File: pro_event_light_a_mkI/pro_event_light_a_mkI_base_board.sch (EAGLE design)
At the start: 29 parts, among them IC1 ILD4001, IC2 ILD4001, IC3 ILD4001, IC4 ILD4001

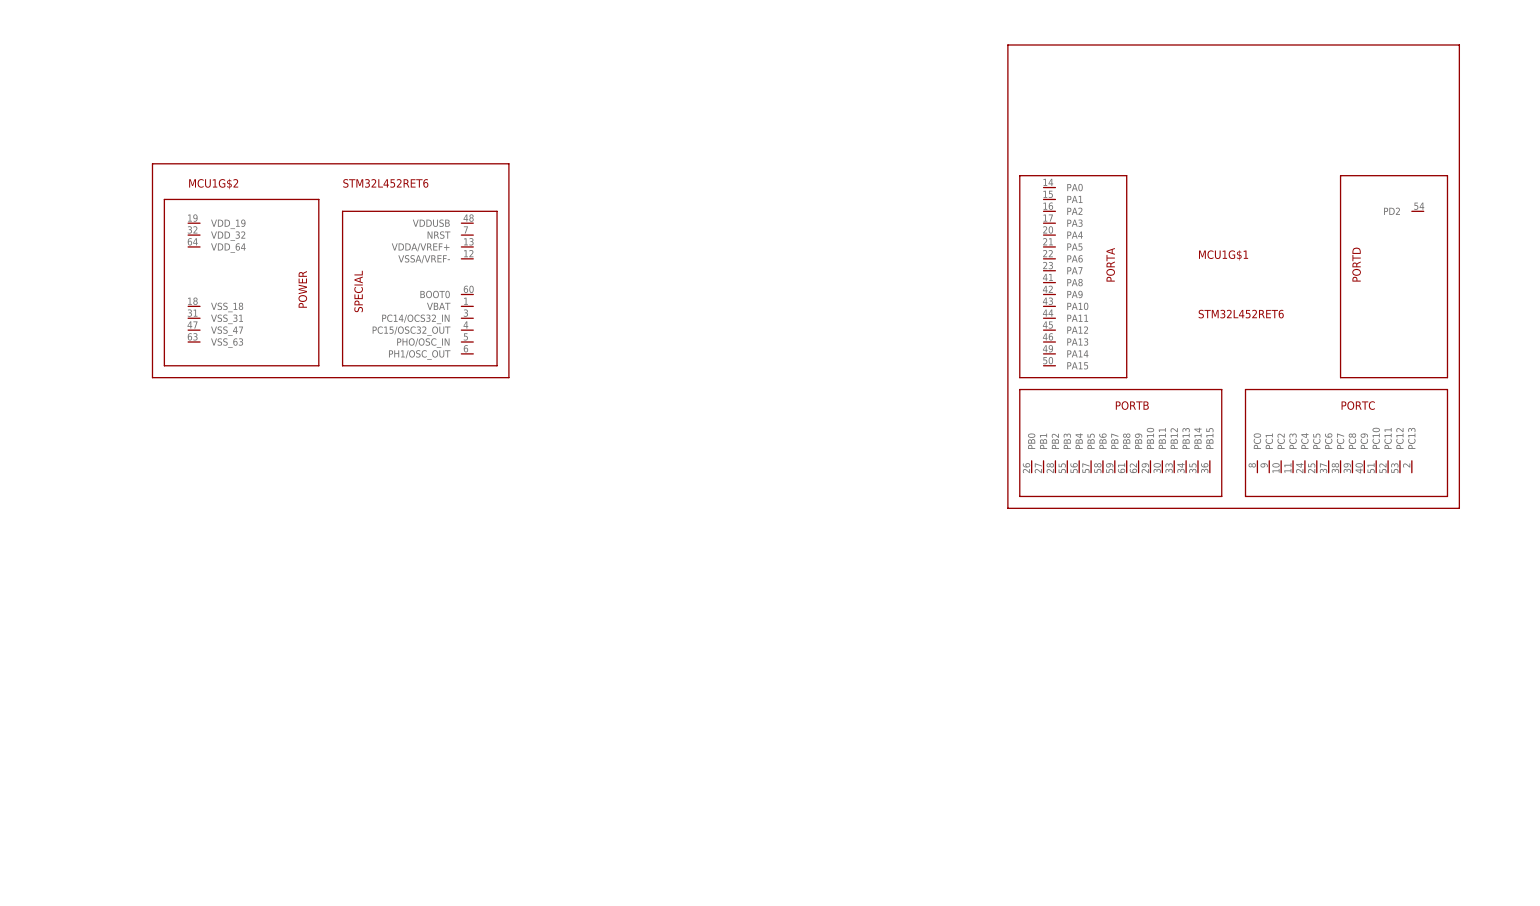
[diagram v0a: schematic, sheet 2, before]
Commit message: included rotary switch (also in separate library)
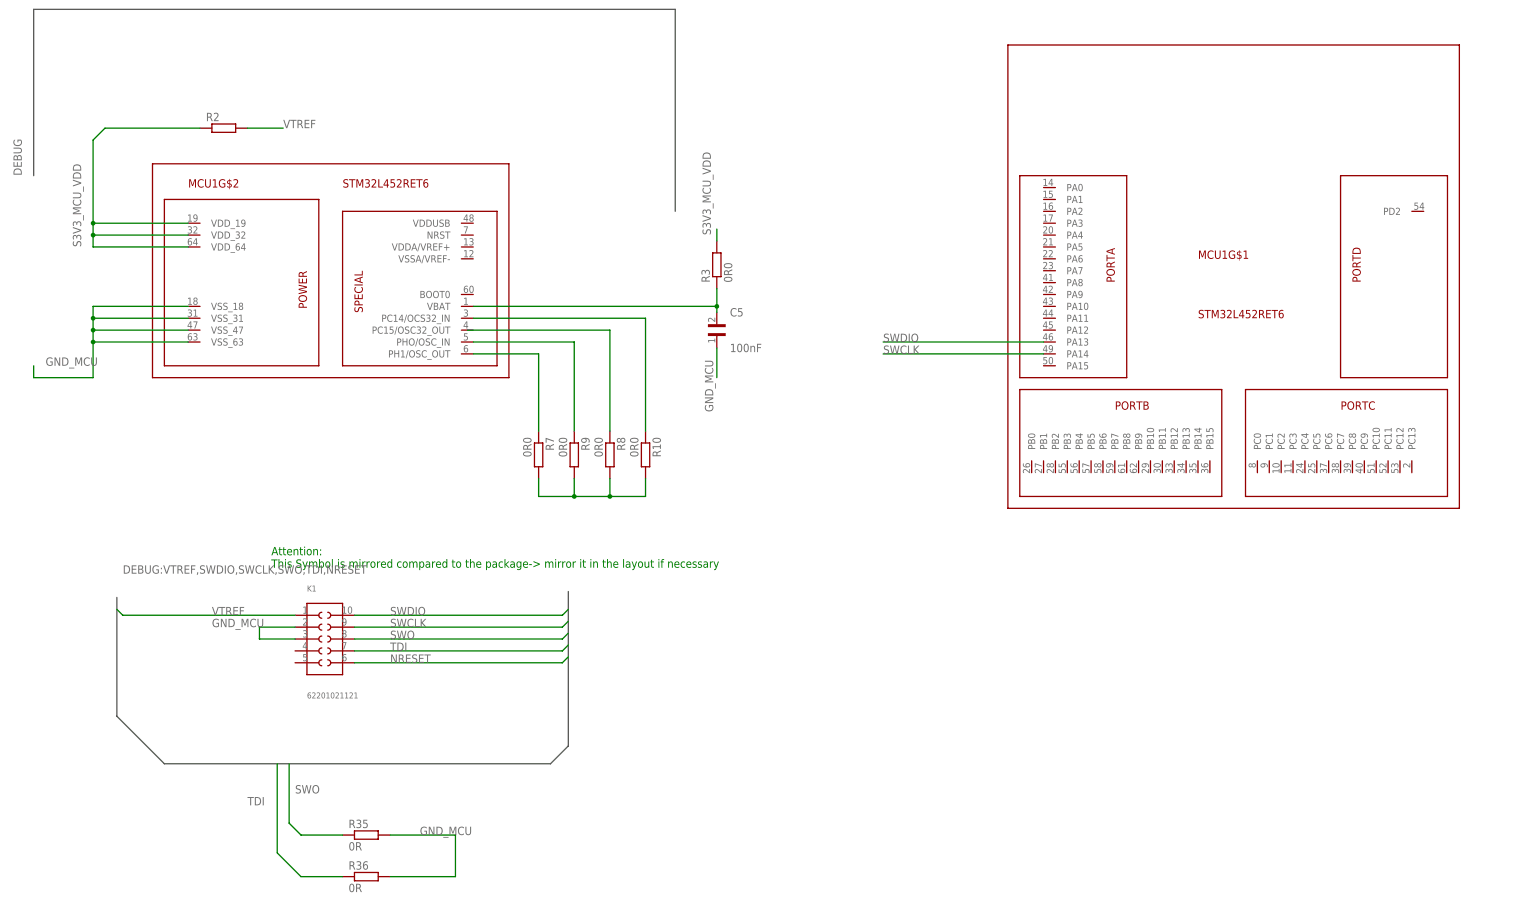
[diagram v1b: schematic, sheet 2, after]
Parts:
- added C1, C29, C34, C35: 1uF, Eagle_Wurth_Elektronik_Passive_Capacitors_rev15a:WCAP-CSGP_1206
- added C5: 100nF, Eagle_Wurth_Elektronik_Passive_Capacitors_rev15a:WCAP-CSGP_0603-REFLOW
- added K1: 62201021121, Board_to_Board_Connectors_rev15d:62201021121
- added R10, R3, R7, R8, R9: 0R0, rcl:R-EU_R0603
- added R2: (no value), rcl:R-EU_R0603
- added R35, R36: 0R, rcl:R-EU_R0603
- added U$10, U$11, U$15, U$8: (no value), mod-eagle_library_standard_passive_parts:PCB_MOUNTING_HOLES_M3
- added U$7: ALPS_EC11D, mod_eagle_library_switches:ALPS_EC11D
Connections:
- new net GND_MCU: C1.2, C29.2, C34.2, C35.2, C5.1, K1.2, K1.3, MCU1G$2.VSS_18, MCU1G$2.VSS_47, MCU1G$2.VSS_63, R10.2, R35.2, R36.2, R7.2, R8.2, R9.2
- new net N$15: C34.1, U$10.1
- new net N$17: C35.1, U$15.1
- new net N$18: C1.1, U$8.1
- new net N$19: C5.2, MCU1G$2.VBAT, R3.1
- new net N$20: MCU1G$2.PC14/OCS32_IN, R10.1
- new net N$21: R8.1
- new net N$26: MCU1G$2.PHO/OSC_IN, R9.1
- new net N$27: MCU1G$2.PH1/OSC_OUT, R7.1
- new net N$9: C29.1, U$11.1
- new net NRESET: K1.6
- new net S3V3_MCU_VDD: MCU1G$2.VDD_19, MCU1G$2.VDD_32, MCU1G$2.VDD_64, R2.1, R3.2
- new net SWCLK: K1.9, MCU1G$1.PA14
- new net SWDIO: K1.10, MCU1G$1.PA13
- new net SWO: K1.8, R35.1
- new net TDI: K1.7, R36.1
- new net VTREF: K1.1, R2.2
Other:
- note added: "Attention: This Symbol is mirrored compared to the package-> mirror it in the layout if necessary"

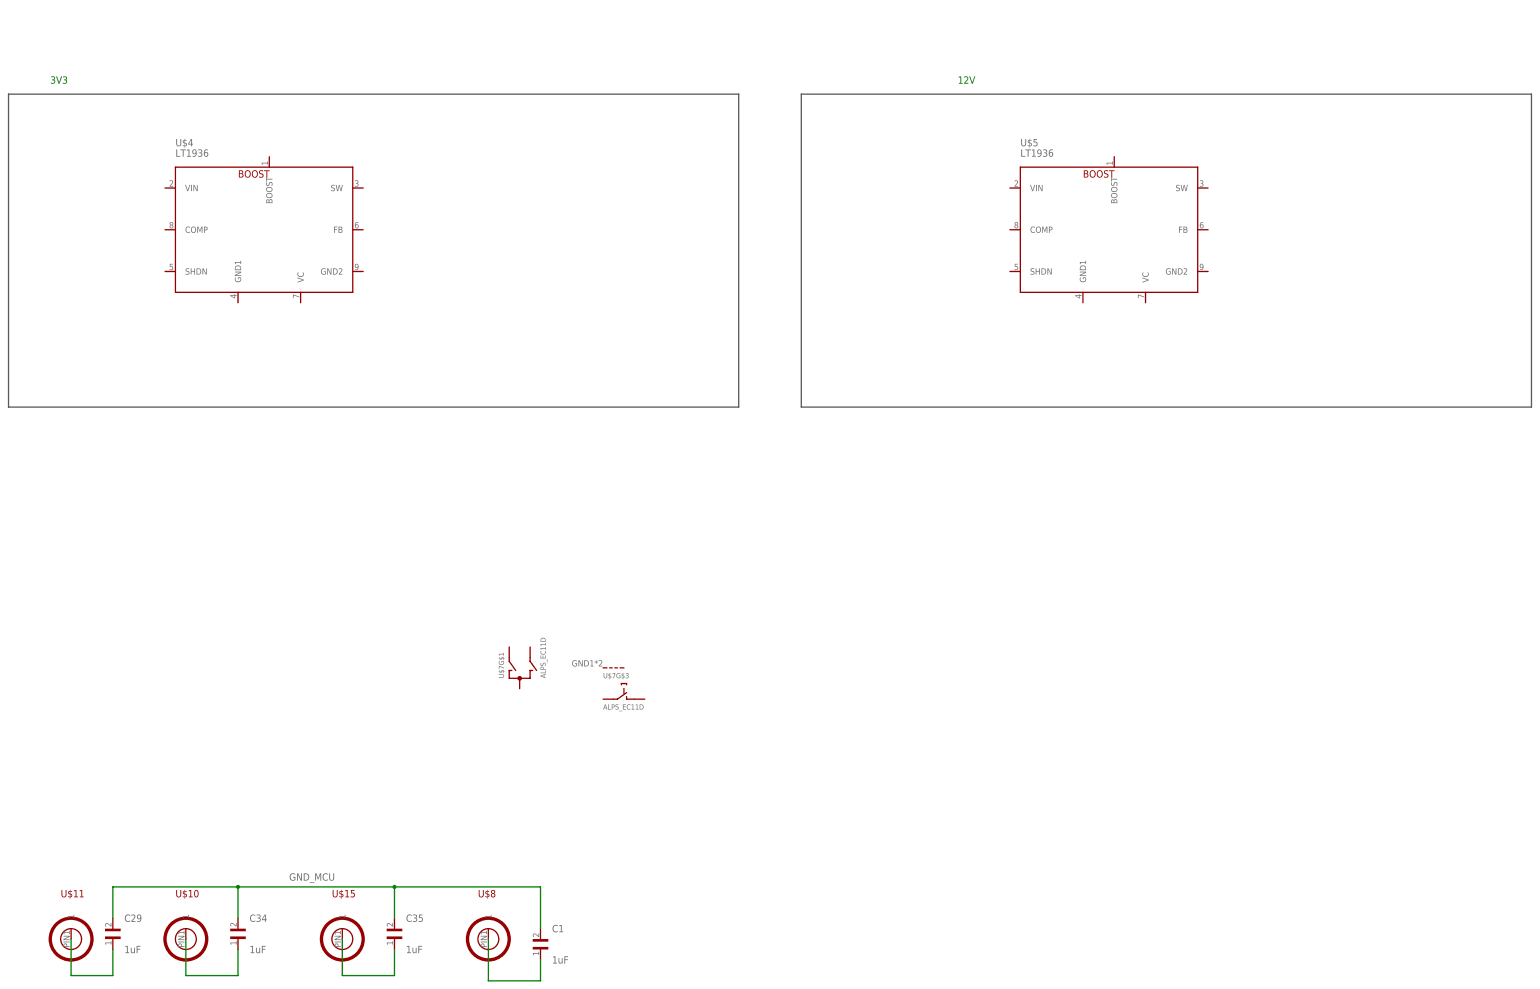
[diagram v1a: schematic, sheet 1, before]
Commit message: some comments and periphery on LT1936
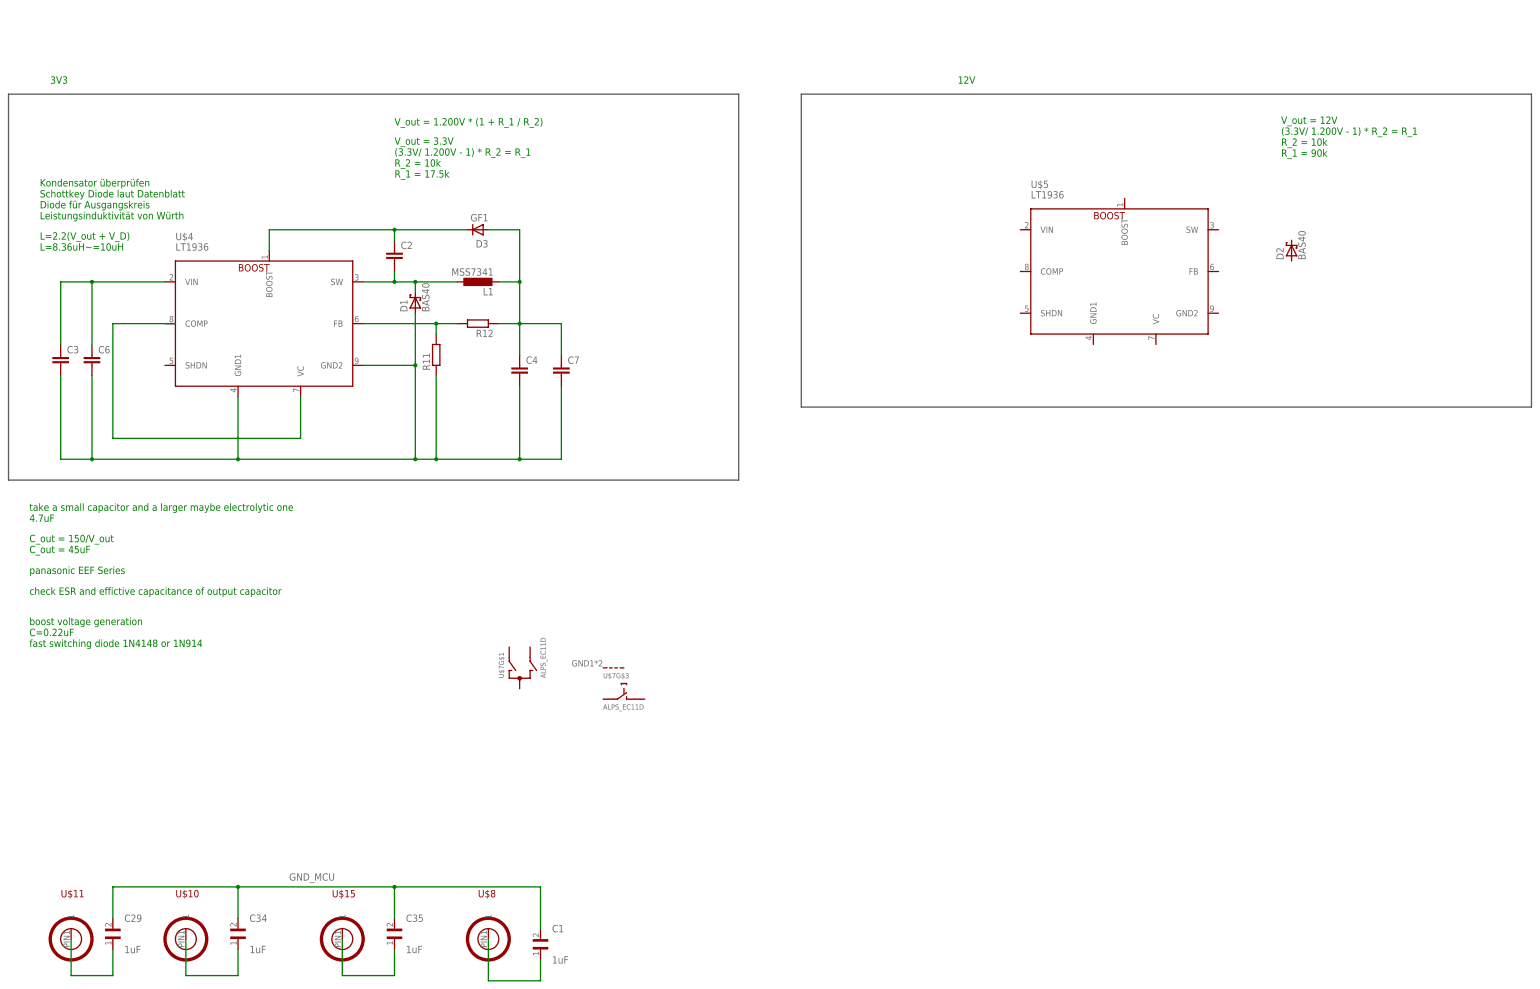
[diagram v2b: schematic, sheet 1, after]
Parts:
- added C2, C3, C4, C6, C7: (no value), rcl:C-EUC0603
- added D1, D2: BAS40, diode:BAS40
- added D3: GF1, diode:GF1
- added L1: MSS7341, inductor-coilcraft:MSS7341
- added R11, R12: (no value), rcl:R-EU_R0603
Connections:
- new net N$28: U$4.VC
- new net N$30: C3.1, C6.1, U$4.VIN
- new net N$33: C2.1, D3.C, U$4.BOOST
- new net N$34: C2.2, D1.C, L1.2, U$4.SW
- new net N$35: R11.2, R12.2, U$4.FB
- new net N$36: C4.1, C7.1, D3.A, L1.1, R12.1
- net GND_MCU: now also C3.2, C4.2, C6.2, C7.2, D1.A, R11.1, U$4.GND1, U$4.GND2
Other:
- note added: "C_out = 150/V_out C_out = 45uF"
- note added: "Kondensator überprüfen Schottkey Diode laut Datenblatt Diode für Ausgangskreis Leistungsinduktivität von Würth"
- note added: "L=2.2(V_out + V_D) L=8.36uH~=10uH"
- note added: "V_out = 1.200V * (1 + R_1 / R_2)"
- note added: "V_out = 12V (3.3V/ 1.200V - 1) * R_2 = R_1 R_2 = 10k R_1 = 90k"
- note added: "V_out = 3.3V (3.3V/ 1.200V - 1) * R_2 = R_1 R_2 = 10k R_1 = 17.5k"
- note added: "boost voltage generation C=0.22uF fast switching diode 1N4148 or 1N914"
- note added: "check ESR and effictive capacitance of output capacitor"
- note added: "panasonic EEF Series"
- note added: "take a small capacitor and a larger maybe electrolytic one 4.7uF"
- moved on the sheet: U$4, U$5

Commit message: commit prior of trying to clone some parts
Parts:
- removed IC1, IC2, IC3, IC4: ILD4001, infineon:ILD4001
- removed U$1, U$2, U$3, U$6: PMXB56EN, mod_eagle_library_discrete_elements:PMXB56EN
- removed U$5: LT1936, mod_eagle_library_pmic:LT1936
- added C10: 10uF, Eagle_Wurth_Elektronik_Passive_Capacitors_rev15a:WCAP-ASNP_4X5.5(DXL)
- added C8/1: (no value), Eagle_Wurth_Elektronik_Passive_Capacitors_rev15a:WCAP-CSGP_0603-WAVE
- added DZ1/1: MBR0540T1, mod_eagle_library_discrete_elements:MBR0540T1
- added IC1/1: ILD4001, infineon:ILD4001
- added L2/1: 68uH, EagleLibrary_Wuerth_Elektronik_eiSos_rev16a:WE-LQ_1210
- added R13: 27K, rcl:R-EU_R0603
- added R14/1: (no value), rcl:R-EU_R0603
- added U1/1: PMXB56EN, mod_eagle_library_discrete_elements:PMXB56EN
- C2: value (none) -> 220pF; device rcl:C-EUC0603 -> Eagle_Wurth_Elektronik_Passive_Capacitors_rev15a:WCAP-CSGP_0603-WAVE
- C3: value (none) -> 45uF; device rcl:C-EUC0603 -> Eagle_Wurth_Elektronik_Passive_Capacitors_rev15a:WCAP-ASNP_4X5.5(DXL)
- C4, C6, C7: value (none) -> 4.7uF; device rcl:C-EUC0603 -> Eagle_Wurth_Elektronik_Passive_Capacitors_rev15a:WCAP-CSGP_0603-WAVE
- D1, D2: value BAS40 -> MBR0540T1; device diode:BAS40 -> mod_eagle_library_discrete_elements:MBR0540T1
- D3: value GF1 -> 1N4148WS; device diode:GF1 -> mod_eagle_library_discrete_elements:1N4148WS
- L1: value MSS7341 -> 1uH; device inductor-coilcraft:MSS7341 -> EagleLibrary_Wuerth_Elektronik_eiSos_rev16a:WE-LQ_1210
- R11: value (none) -> 10K
- R12: value (none) -> 17K5
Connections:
- net N$16 renamed VSENSE_LEDR
- net N$2 renamed VSENSE_LEDG
- net N$23 renamed VSENSE_LEDW
- net N$5 renamed VSENSE_LEDB
- removed net N$1: U$1.S, U$2.S, U$3.S
- removed net N$10: R5.2
- removed net N$11: R6.2
- removed net N$13: R4.2
- removed net N$22: LEDR2.P$2, LEDR4.P$2, LEDR6.P$2, U$2.D
- removed net N$24: LEDW2.P$2, U$6.D
- removed net N$31: LEDB2.P$2, LEDB4.P$2, U$3.D
- removed net N$36: C4.1, C7.1, D3.A, L1.1, R12.1
- removed net N$8: R1.2
- new net DRIVER_LEDB: LEDB2.P$2, LEDB4.P$2
- new net DRIVER_LEDG: LEDG1.P$2
- new net DRIVER_LEDG/1: L2/1.1
- new net DRIVER_LEDR: LEDR2.P$2, LEDR4.P$2, LEDR6.P$2
- new net DRIVER_LEDW: LEDW2.P$2
- new net ENABLE_LEDG/1: IC1/1.EN/PWM
- new net N$2: IC1/1.VDRIVE, R14/1.2, U1/1.G
- new net SUPPLY_24V: C10.2, C6.1, C8/1.2, D2.C, DZ1/1.C, IC1/1.VS, R1.2, R13.2, R4.2, R5.2, R6.2, U$4.VIN
- new net SUPPLY_3V3: C3.2, C4.1, D3.A, L1.2, R12.1
- new net VIN: D2.A
- new net VSENSE_LEDG/1: IC1/1.VSENSE
- net GND_MCU: now also C10.1, C3.1, C8/1.1, IC1/1.GND, R14/1.1, U1/1.S; no longer C3.2
- net N$28: now also U$4.COMP
- net N$29: now also DZ1/1.A, L2/1.2, U1/1.D; no longer LEDG1.P$2, U$1.D
- net N$30: now also C7.1, R13.1, U$4.SHDN; no longer C3.1, C6.1, U$4.VIN
- net N$34: now also L1.1; no longer L1.2
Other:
- note added: "LEDG"
- note removed: "Kondensator überprüfen Schottkey Diode laut Datenblatt Diode für Ausgangskreis Leistungsinduktivität von Würth"
- note removed: "check ESR and effictive capacitance of output capacitor"
- note removed: "panasonic EEF Series"
- moved on the sheet: C2, C3, C4, C6, C7, LEDB1, LEDB2, LEDB3, LEDB4, LEDG1, LEDG2, LEDR1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

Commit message: first attempt using modules
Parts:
- removed C10: 10uF, Eagle_Wurth_Elektronik_Passive_Capacitors_rev15a:WCAP-ASNP_4X5.5(DXL)
- removed C6, C7: 4.7uF, Eagle_Wurth_Elektronik_Passive_Capacitors_rev15a:WCAP-CSGP_0603-WAVE
- removed C8/1: (no value), Eagle_Wurth_Elektronik_Passive_Capacitors_rev15a:WCAP-CSGP_0603-WAVE
- removed D1, DZ1/1: MBR0540T1, mod_eagle_library_discrete_elements:MBR0540T1
- removed D3: 1N4148WS, mod_eagle_library_discrete_elements:1N4148WS
- removed IC1/1: ILD4001, infineon:ILD4001
- removed L1: 1uH, EagleLibrary_Wuerth_Elektronik_eiSos_rev16a:WE-LQ_1210
- removed L2/1: 68uH, EagleLibrary_Wuerth_Elektronik_eiSos_rev16a:WE-LQ_1210
- removed R14/1: (no value), rcl:R-EU_R0603
- removed U$4: LT1936, mod_eagle_library_pmic:LT1936
- removed U$7: ALPS_EC11D, mod_eagle_library_switches:ALPS_EC11D
- removed U1/1: PMXB56EN, mod_eagle_library_discrete_elements:PMXB56EN
- added R14, R15, R16: 100, rcl:R-EU_R0603
- added SW1: ALPS_EC11D, mod_eagle_library_switches:ALPS_EC11D
- C2: value 220pF -> 4.7pF
- C3: value 45uF -> 4.7pF; device Eagle_Wurth_Elektronik_Passive_Capacitors_rev15a:WCAP-ASNP_4X5.5(DXL) -> Eagle_Wurth_Elektronik_Passive_Capacitors_rev15a:WCAP-CSGP_0603-WAVE
- C4: value 4.7uF -> 4.7pF
- R11: value 10K -> 22K
- R12: value 17K5 -> 22K
- R13: value 27K -> 22K
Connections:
- removed net DRIVER_LEDG/1: L2/1.1
- removed net ENABLE_LEDG/1: IC1/1.EN/PWM
- removed net N$28: U$4.COMP, U$4.VC
- removed net N$29: DZ1/1.A, L2/1.2, U1/1.D
- removed net VSENSE_LEDG/1: IC1/1.VSENSE
- new net N$1: R11.1, R14.1, SW1G$1.A
- new net N$10: R11.2, R12.2, R13.2
- new net N$11: C3.2, R15.1
- new net N$13: C2.2, R14.2
- new net N$16: R13.1, R16.2, SW1G$3.E
- new net N$5: C2.1, C3.1, C4.1, SW1G$1.C, SW1G$2.G, SW1G$3.D
- new net N$8: C4.2, R16.1
- net GND_MCU: now also R14.1; no longer C10.1, C6.2, C7.2, C8/1.1, D1.A, IC1/1.GND, R14/1.1, U$4.GND1, U$4.GND2, U1/1.S
- net N$2: now also R12.1, R14.2, R15.2, SW1G$1.B; no longer IC1/1.VDRIVE, R14/1.2, U1/1.G
- net N$30: no longer C7.1, U$4.SHDN
- net N$33: no longer D3.C, U$4.BOOST
- net N$34: no longer D1.C, L1.1, U$4.SW
- net N$35: no longer U$4.FB
- net SUPPLY_24V: no longer C10.2, C6.1, C8/1.2, DZ1/1.C, IC1/1.VS, U$4.VIN
- net SUPPLY_3V3: no longer D3.A, L1.2
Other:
- note added: "LED"
- note removed: "12V"
- note removed: "V_out = 12V (3.3V/ 1.200V - 1) * R_2 = R_1 R_2 = 10k R_1 = 90k"
- moved on the sheet: C2, C3, C4, R11, R12, R13

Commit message: preliminary layout for LT1936
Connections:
- net N$33 renamed PMIC_LT1936_BOOST
- net N$34 renamed PMIC_LT1936_SW
- net SUPPLY_3V3 renamed PMIC_LT1936_VOUT
- new net LEDB: MCU1G$1.PB14
- new net LEDG: MCU1G$1.PB15
- new net LEDR: MCU1G$1.PB13
- new net LEDW: MCU1G$1.PB12
- new net PMIC_IL4001_GND: R14.1
- new net PMIC_LT1936_GND: C3.1, C4.2, R11.1
- new net PMIC_LT1936_VIN: R13.2
- net GND_MCU: no longer C3.1, C4.2, R11.1, R14.1
- net SUPPLY_24V: no longer R13.2
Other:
- moved on the sheet: R11, R12
